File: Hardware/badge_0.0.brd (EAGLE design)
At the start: 100 x 50 mm, 46 parts, among them CON1 PH_2, IC1 CP2102, SW1 MK12C02, SW2 MK12C02, U4 MCP73832T-2DCI/OT

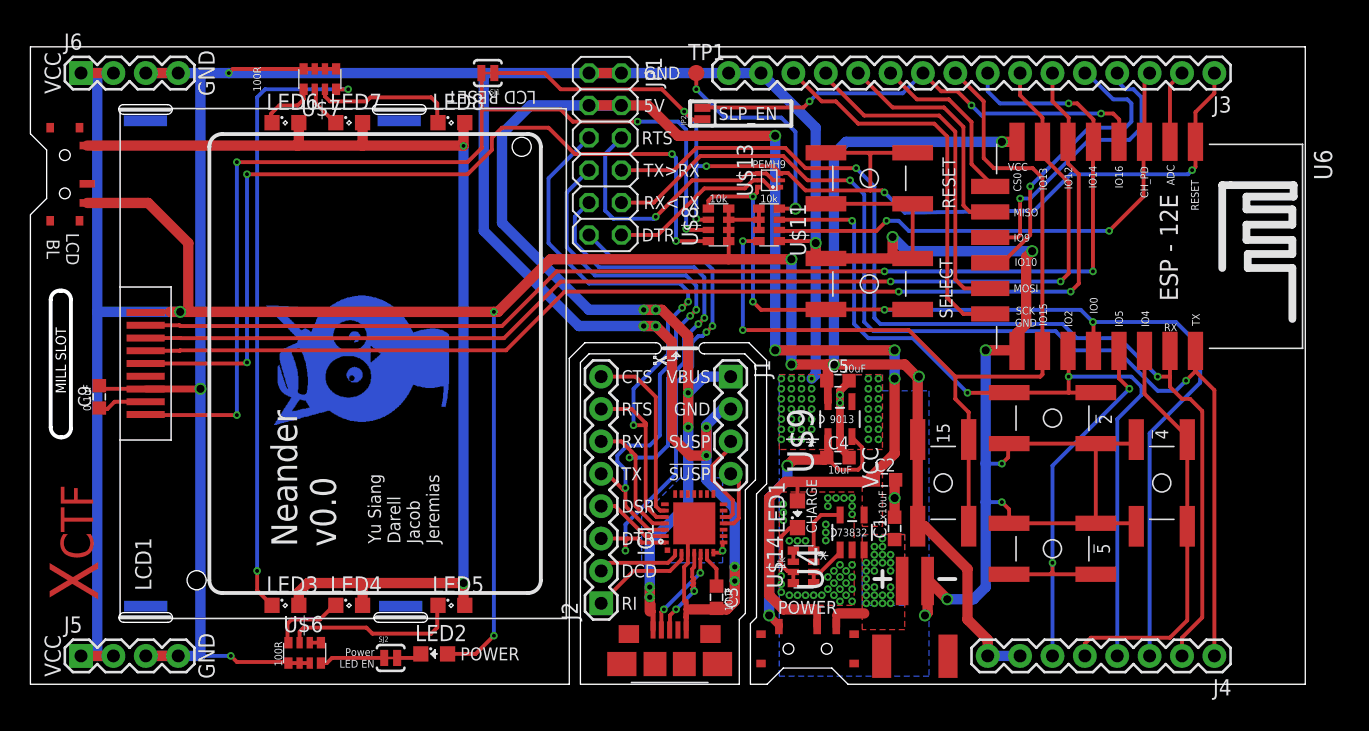
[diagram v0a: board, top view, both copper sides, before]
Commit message: Fixed most of the errors, optimized some traces
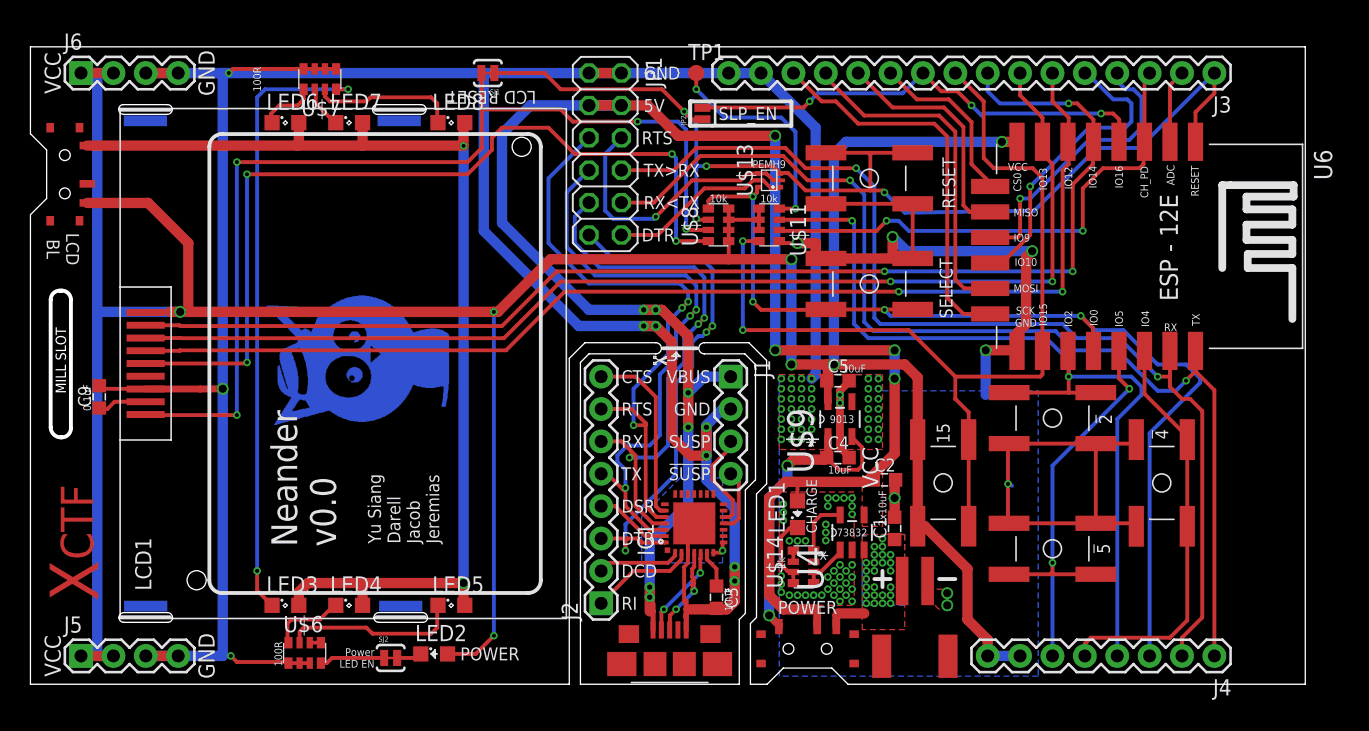
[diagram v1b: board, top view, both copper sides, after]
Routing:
- net GND: track 351.6 -> 334.1 mm, vias 101 -> 100
- net GPIO2/SDA: track 66.9 -> 71.8 mm, vias 3 -> 2
- net RESET: track 87.6 -> 90.1 mm, vias 5 -> 4
- net GPIO13/SPI_SI: track 91.8 -> 90.4 mm
- net GPIO12/SPI_SO: track 92.8 -> 91.8 mm
- net GPIO14/SPI_CLK/SCL: track 98.7 -> 97.7 mm
- net GPIO0: track 80.4 -> 79.8 mm
- net VCC: track 247.4 -> 247.2 mm, vias 8 -> 7

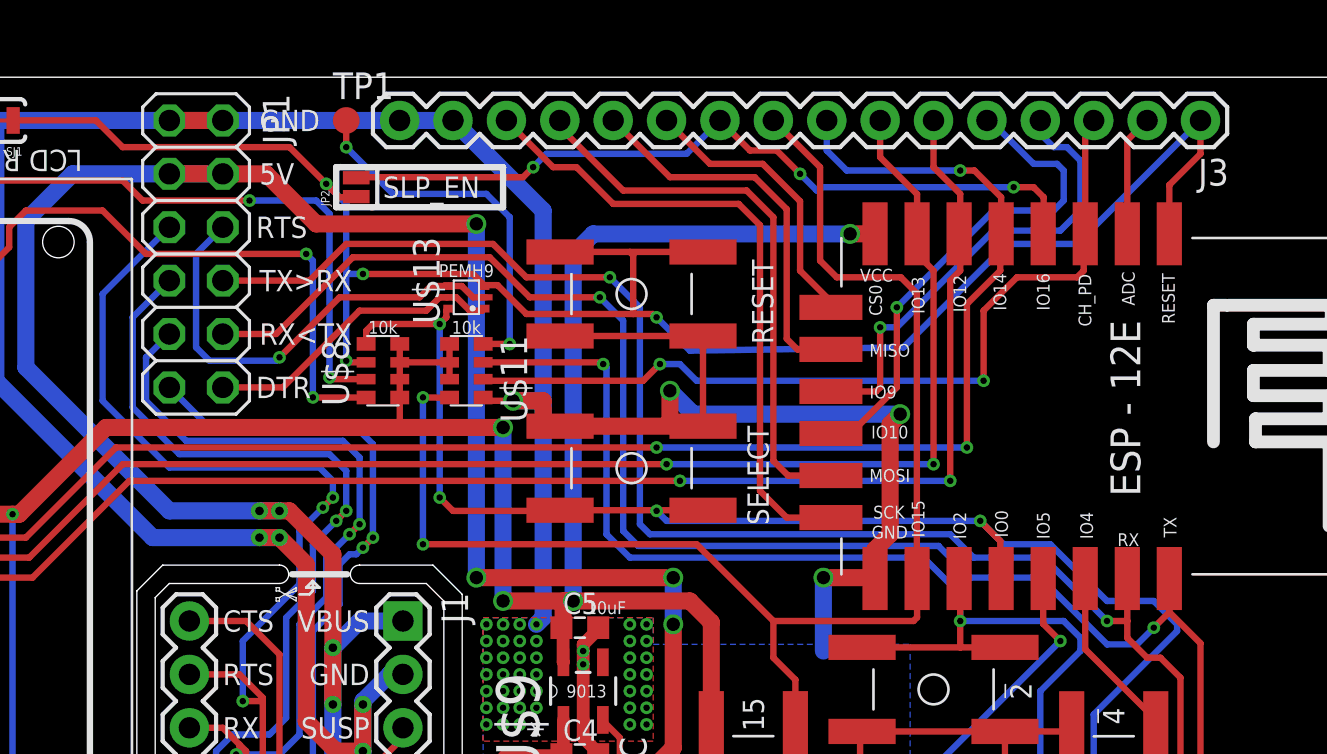
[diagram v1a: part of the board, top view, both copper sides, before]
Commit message: added decoup cap; antenna gnd plane; minor edits;
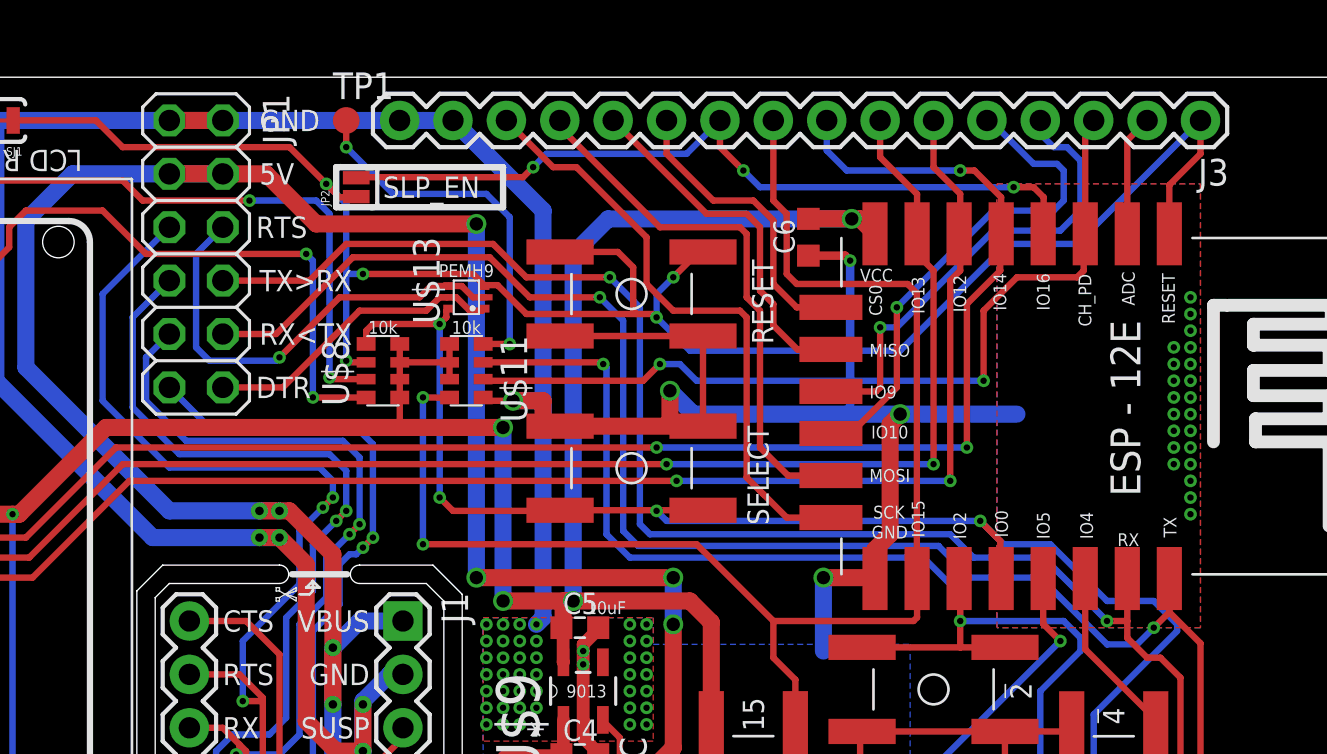
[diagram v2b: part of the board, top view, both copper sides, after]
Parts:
- added C6: 10uF, resistor:C0603K
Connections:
- net GND: now also C6.1
- net VCC: now also C6.2
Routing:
- net GND: track 334.1 -> 349.1 mm, vias 100 -> 123
- net VCC: track 247.2 -> 249.9 mm
- net SCLK: track 30.7 -> 29.0 mm
- net GPIO15/SPI_CS: track 73.8 -> 75.1 mm
- net MISO: track 18.5 -> 17.2 mm
- net MOSI: track 26.9 -> 25.7 mm
- net CS0: track 13.6 -> 14.5 mm
- net GPIO16: track 37.2 -> 37.8 mm
- net RESET: track 90.1 -> 90.6 mm, vias 4 -> 5

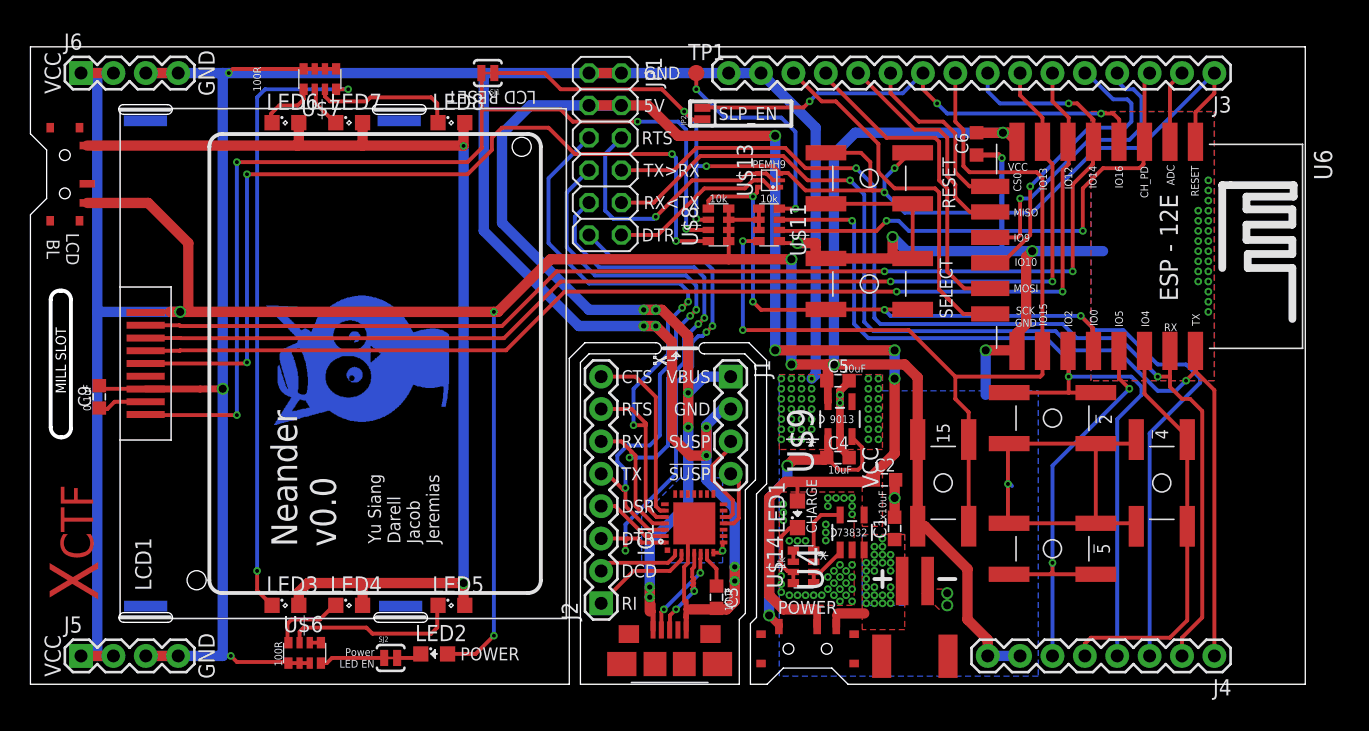
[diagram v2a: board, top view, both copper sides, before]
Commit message: added text to bottom layer; mitred edges;
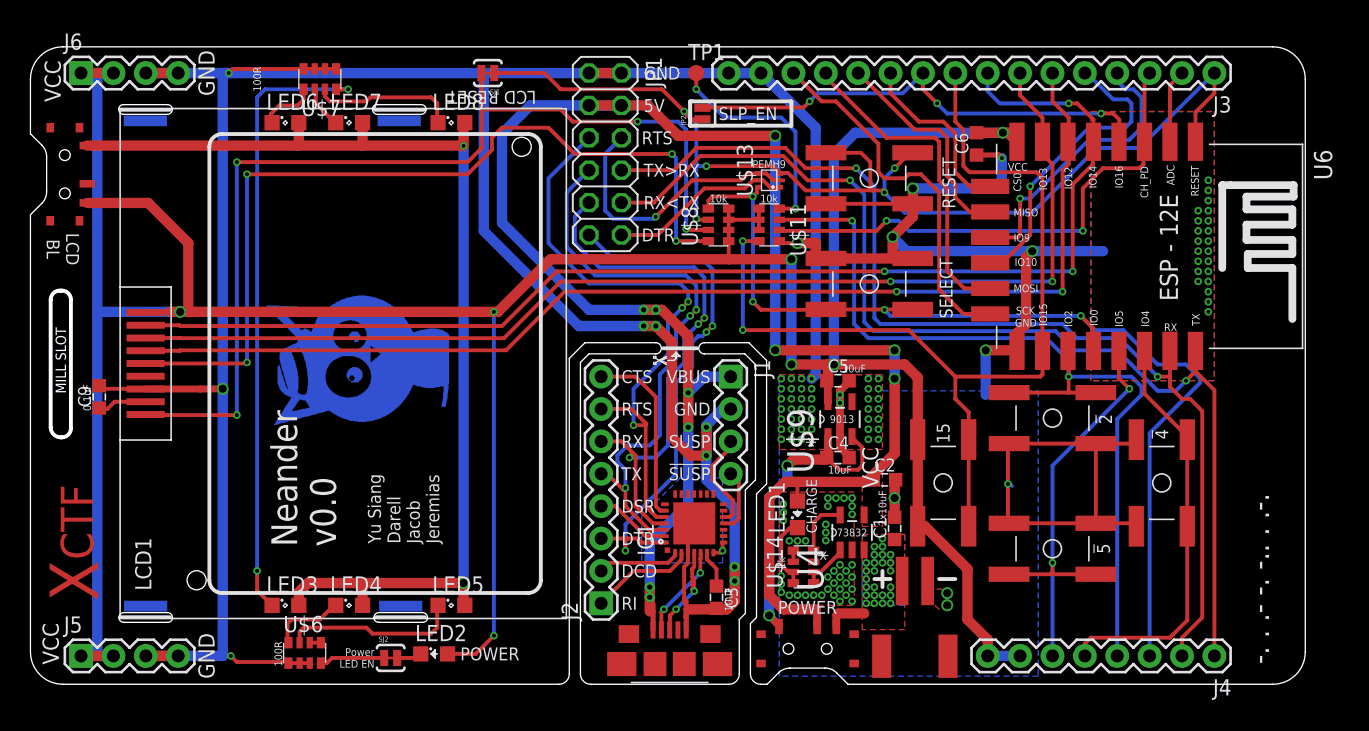
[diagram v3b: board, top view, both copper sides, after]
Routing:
- net GND: track 349.1 -> 351.1 mm, vias 123 -> 124
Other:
- outline, holes or cut-outs redrawn
- board text added: "-. . .- -. -.. . .-."
- board text added: "-..- -.-. - ..-."
